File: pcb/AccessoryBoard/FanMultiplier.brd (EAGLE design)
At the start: 92.1 x 33.7 mm, 22 parts

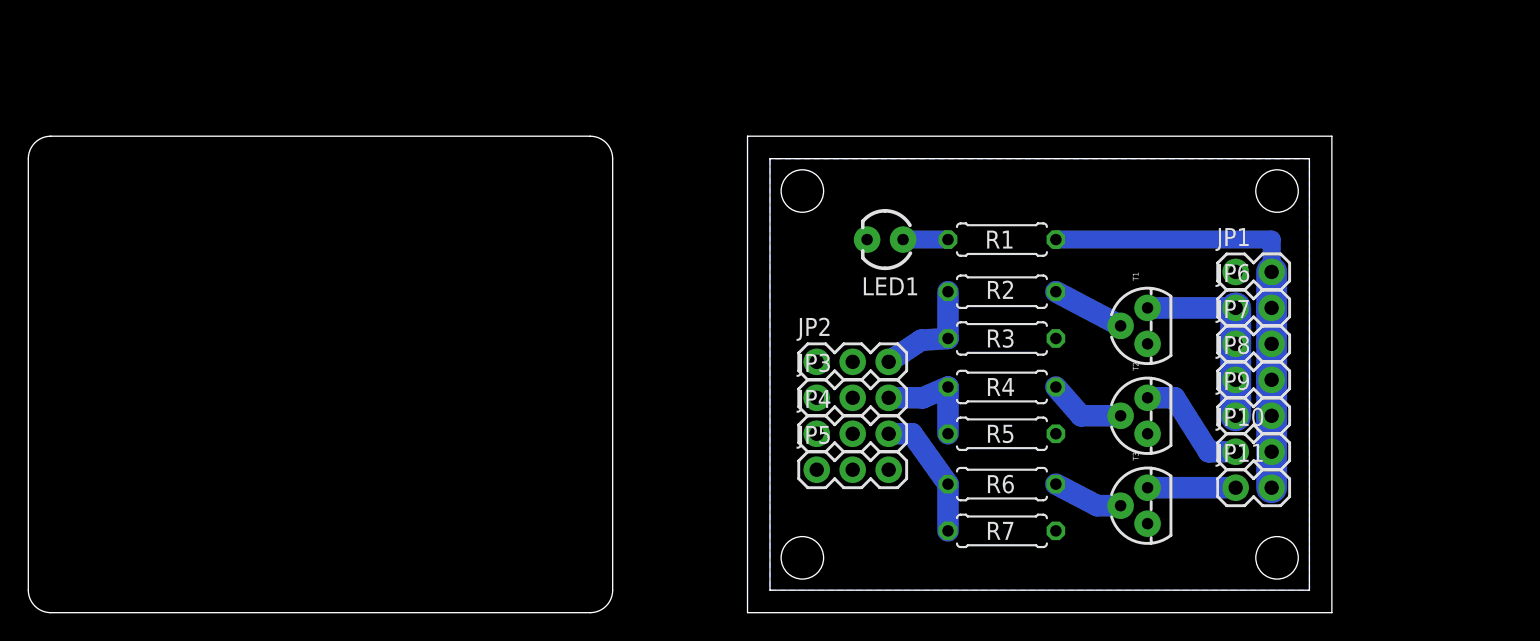
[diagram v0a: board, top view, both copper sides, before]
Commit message: added vcc outputs added 4th pwm output
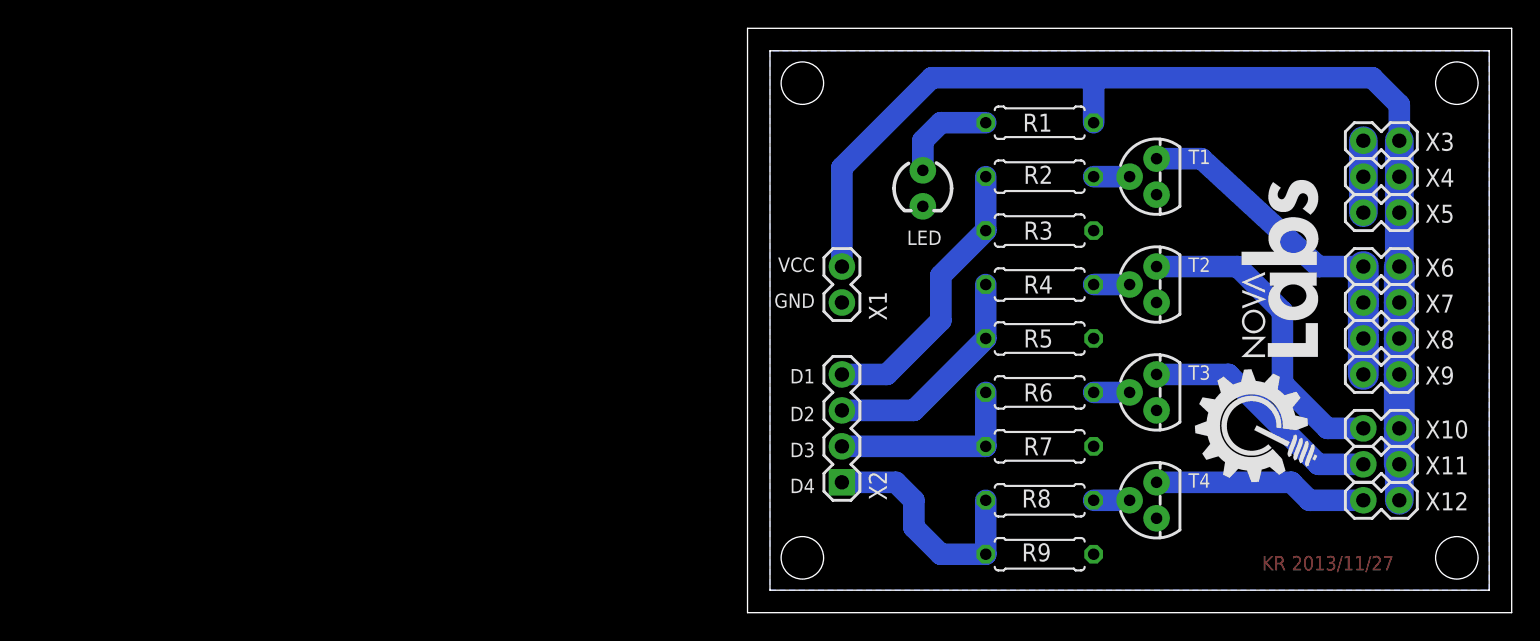
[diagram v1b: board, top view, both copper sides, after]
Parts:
- removed JP1, JP10, JP11, JP6, JP7, JP8, JP9: M02PTH, SparkFun-Connectors:1X02
- removed JP2, JP3, JP4, JP5: (no value), SparkFun-Connectors:1X03
- removed LED1: (no value), SparkFun-LED:LED3MM
- added LED: (no value), SparkFun-LED:LED3MM
- added R8: 100, rcl:0207/7
- added R9: 10k, rcl:0207/7
- added T4: (no value), SparkFun-DiscreteSemi:TO-92
- added U$1: (no value), NOVA-LABS-LOGO:NOVA-LABS-LOGO-FULL-SMALL
- added X1, X10, X11, X12, X3, X4, X5, X6, X7, X8, X9: M02PTH, SparkFun-Connectors:1X02
- added X2: (no value), SparkFun-Connectors:1X04
- R1: value 330 -> 33k
- moved T1 10.6 mm to (27.3, 29.2)
- moved T2 9.29 mm to (27.3, 21.6)
- moved R1 8.68 mm to (19.1, 33.0)
- moved R2 8.55 mm to (19.1, 29.2)
- moved R3 8.07 mm to (19.1, 25.4)
- moved T3 8.03 mm to (27.3, 14.0)
- moved R4 7.71 mm to (19.1, 21.6)
- moved R5 7.24 mm to (19.1, 17.8)
- moved R6 7.00 mm to (19.1, 14.0)
- moved R7 6.54 mm to (19.1, 10.2)
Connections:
- new net N$11: R8.2, T4.2
- new net N$12: T4.3, X12.1
- net GND: now also LED.K, R9.2, T4.1, X1.1, X3.1, X4.1, X5.1; no longer JP1.1, JP2.1, JP3.1, JP4.1, JP5.1, LED1.K
- net N$14: now also X6.1, X7.1, X8.1, X9.1; no longer JP6.1, JP7.1, JP8.1, JP9.1
- net N$16: now also X10.1; no longer JP10.1
- net N$17: now also X11.1; no longer JP11.1
- net N$4: now also LED.A; no longer LED1.A
- net N$5: now also X2.4; no longer JP2.3
- net N$6: now also X2.3; no longer JP3.3
- net N$7: now also X2.2; no longer JP4.3
- net N$8: now also R8.1, R9.1, X2.1; no longer JP2.2, JP3.2, JP4.2, JP5.2
- net VCC: now also X1.2, X10.2, X11.2, X12.2, X3.2, X4.2, X5.2, X6.2, X7.2, X8.2, X9.2; no longer JP1.2, JP10.2, JP11.2, JP6.2, JP7.2, JP8.2, JP9.2
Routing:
- net VCC: track 32.8 -> 80.9 mm
- net N$8: track 0.00 -> 17.2 mm
- net N$12: track 0.00 -> 15.1 mm
- net N$16: track 8.32 -> 22.3 mm
- net N$5: track 7.96 -> 20.0 mm
- net N$14: track 13.8 -> 25.2 mm
- net N$17: track 6.22 -> 17.2 mm
- net N$6: track 7.65 -> 16.1 mm
- net GND: track 0.00 -> 5.08 mm
- net N$7: track 9.32 -> 14.0 mm
- net N$4: track 3.18 -> 7.07 mm
- net N$2: track 5.49 -> 2.54 mm
- net N$1: track 5.17 -> 2.54 mm
- net N$11: track 0.00 -> 2.54 mm
- net N$3: track 4.95 -> 2.54 mm
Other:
- board size 92.1 x 33.7 mm -> 54 x 41.3 mm
- board text added: "D1"
- board text added: "D2"
- board text added: "D3"
- board text added: "D4"
- board text added: "GND"
- board text added: "KR 2013/11/27"
- board text added: "VCC"

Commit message: minor routing improvements
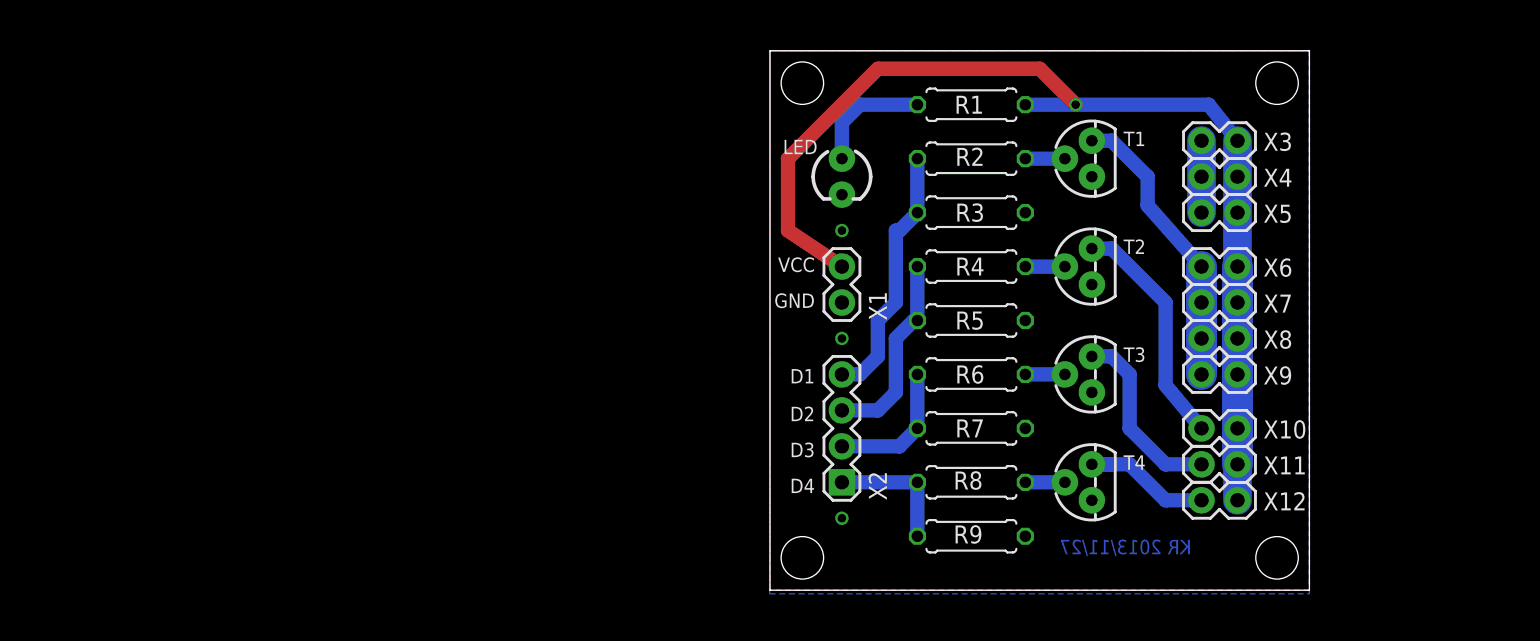
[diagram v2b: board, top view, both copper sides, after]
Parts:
- removed U$1: (no value), NOVA-LABS-LOGO:NOVA-LABS-LOGO-FULL-SMALL
- moved X10 11.4 mm to (30.5, 11.4)
- moved X11 11.4 mm to (30.5, 8.89)
- moved X12 11.4 mm to (30.5, 6.35)
- moved X3 11.4 mm to (30.5, 31.8)
- moved X4 11.4 mm to (30.5, 29.2)
- moved X5 11.4 mm to (30.5, 26.7)
- moved X6 11.4 mm to (30.5, 22.9)
- moved X7 11.4 mm to (30.5, 20.3)
- moved X8 11.4 mm to (30.5, 17.8)
- moved X9 11.4 mm to (30.5, 15.2)
- moved LED 5.77 mm to (5.08, 29.2)
- moved R3 4.99 mm to (14.2, 26.7)
- moved R2 4.99 mm to (14.2, 30.5)
- moved R4 4.99 mm to (14.2, 22.9)
- moved R5 4.99 mm to (14.2, 19.1)
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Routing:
- net N$8: track 17.2 -> 9.14 mm
- net N$16: track 22.3 -> 16.6 mm
- net VCC: track 80.9 -> 75.3 mm, vias 0 -> 1
- net N$12: track 15.1 -> 10.2 mm
- net N$14: track 25.2 -> 20.4 mm
- net N$7: track 14.0 -> 9.67 mm
- net N$17: track 17.2 -> 13.1 mm
- net N$6: track 16.1 -> 14.0 mm
- net N$5: track 20.0 -> 18.3 mm
- net N$4: track 7.07 -> 8.40 mm
- added copper zone on layer 1, net GND
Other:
- board size 54 x 41.3 mm -> 38.1 x 38.1 mm
- board text added: "/Users/krad/Documents/My Pictures/NovaLabs/nova-labs_logo_black.bmp"

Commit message: brought headers together for easier soldering replaced logo with text other minor improvements
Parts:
- moved X1 2.54 mm to (5.08, 22.9), turned to 270 degrees
- moved X5 1.27 mm to (30.5, 25.4)
- moved X12 1.27 mm to (30.5, 7.62)
- moved X10 1.27 mm to (30.5, 12.7)
- moved X11 1.27 mm to (30.5, 10.2)
- moved X3 1.27 mm to (30.5, 30.5)
- moved X4 1.27 mm to (30.5, 27.9)
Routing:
- net GND: track 5.08 -> 0.00 mm, vias 0 -> 2
- net N$12: track 10.2 -> 8.27 mm
- net N$14: track 20.4 -> 21.7 mm
- net N$17: track 13.1 -> 12.2 mm
- net N$16: track 16.6 -> 15.8 mm
- net VCC: track 75.3 -> 74.7 mm
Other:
- board text added: "+"
- board text added: "-"
- board text added: "KR 2014/01/11"
- board text added: "Nova Labs Fan Board v4"
- board text added: "xD1"
- board text added: "xD2"
- board text added: "xD3"
- board text added: "xD4"
- board text added: "xVCC"
- board text removed: "KR 2013/11/27"
